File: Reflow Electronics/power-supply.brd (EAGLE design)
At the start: 80 x 64.8 mm, 19 parts, among them IC1 LM2574N-5.0

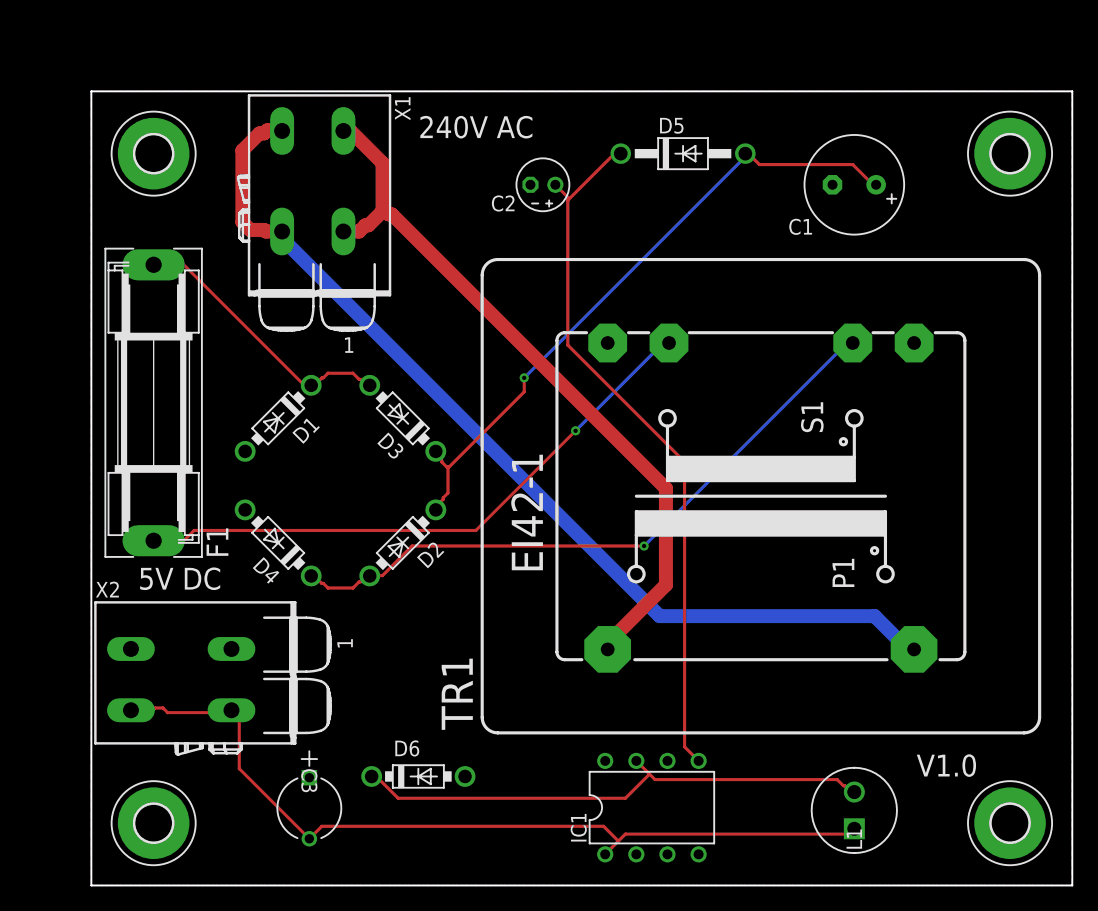
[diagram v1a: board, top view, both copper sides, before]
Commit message: Fixed schematic and board for problems found on first iteration
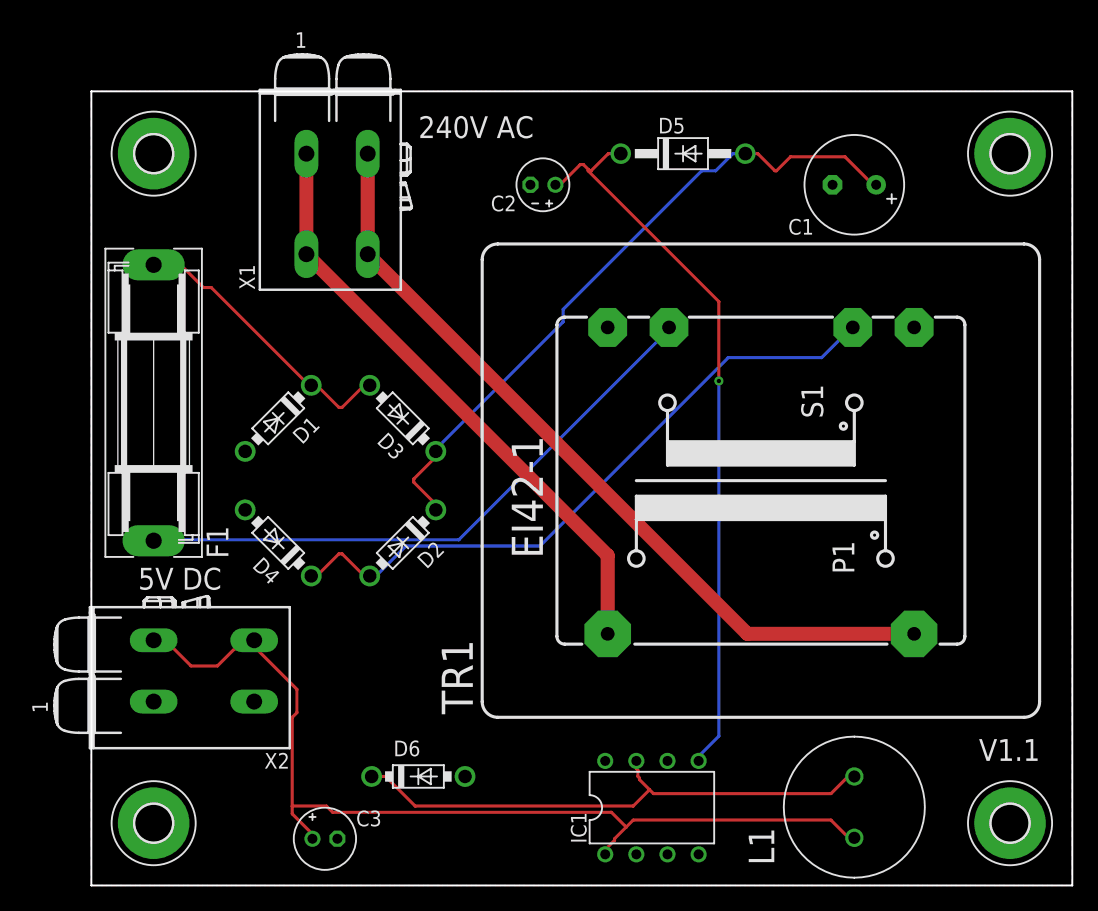
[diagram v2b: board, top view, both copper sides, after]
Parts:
- C3: value MAL203854221E3 -> 220u; device reflow-oven:CAP_5_X_11 -> rcl:E2-5
- L1: value ELC11D331F -> 330UH; device reflow-oven:IND_ELC11D -> Panasonic-ELC:IND_ELC11D
- TR1: value (none) -> 44231
- moved X2 10.9 mm to (5.08, 12.7), turned to 180 degrees
- moved X1 9.92 mm to (15.2, 59.7), turned to 90 degrees
- moved TR1 1.27 mm to (54.6, 33.0)
- moved L1 1.27 mm to (62.2, 8.89)
- moved C3 1.27 mm to (19.1, 3.81), turned to 0 degrees
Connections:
- net 5V400MA: now also C3.+; no longer C3.2
- net GND: now also C3.-; no longer C3.1
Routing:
- net 240VAC-N: track 79.4 -> 65.6 mm
- net 240VAC-L: track 59.7 -> 49.3 mm
- net 5V400MA: track 69.1 -> 79.3 mm
- net N$1: track 57.7 -> 60.1 mm, vias 0 -> 1
- net N$3: track 53.0 -> 55.0 mm, vias 1 -> 0
- net N$6: track 43.1 -> 44.4 mm
- net N$5: track 52.9 -> 54.2 mm, vias 1 -> 0
- net N$4: track 22.6 -> 23.3 mm
- net 12VAC: track 48.8 -> 49.4 mm, vias 1 -> 0
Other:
- board text added: "V1.1"
- board text removed: "V1.0"

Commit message: Tweaked power supply for future following testing. Added BOM.
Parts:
- X1: value (none) -> 2604-1103; device con-wago_2604:P-2604-1102 -> con-wago_2604:P-2604-1103
- moved C2 2.84 mm to (39.4, 55.9)
- moved D5 1.27 mm to (49.5, 59.7)
- moved X1 1.27 mm to (14.0, 59.7)
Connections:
- net GND: now also X1.P3.1, X1.P3.2
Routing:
- net N$3: track 55.0 -> 60.8 mm
- net 12VAC: track 49.4 -> 52.4 mm
- net N$1: track 60.1 -> 57.5 mm
- net N$5: track 54.2 -> 56.1 mm
- net 240VAC-N: track 65.6 -> 66.9 mm
- net 240VAC-L: track 49.3 -> 49.9 mm
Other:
- board text added: "+"
- board text added: "-"
- board text added: "E"
- board text added: "L"
- board text added: "N"
